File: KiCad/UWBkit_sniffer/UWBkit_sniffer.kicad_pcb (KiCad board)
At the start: 4 copper layers, 57.4 x 67.3 mm, 78 parts, among them J1 Conn_I2C1, J10 USB_C_Receptacle_USB2.0_14P, J11 USB_C_Receptacle_USB2.0_14P, J2 Conn_I2C2, J3 Conn_01x03, J4 Conn_SPIS, J5 Conn_SPIM, J6 Conn_SWD, J7 Conn_GPIO, J8 Conn_Coaxial, J9 Conn_01x02, SW1 SW_Push, T1 TestPoint_Small, T10 TestPoint_Small, T11 TestPoint_Small, T12 TestPoint_Small, T2 TestPoint_Small, T3 TestPoint_Small, T4 TestPoint_Small, T5 TestPoint_Small, T6 TestPoint_Small, T7 TestPoint_Small, T8 TestPoint_Small, T9 TestPoint_Small, U1 LBUA5QJ2AB, U2 XC9285B33CMR-G, U3 CP2104, U4 IP4234CZ6, U5 IP4234CZ6

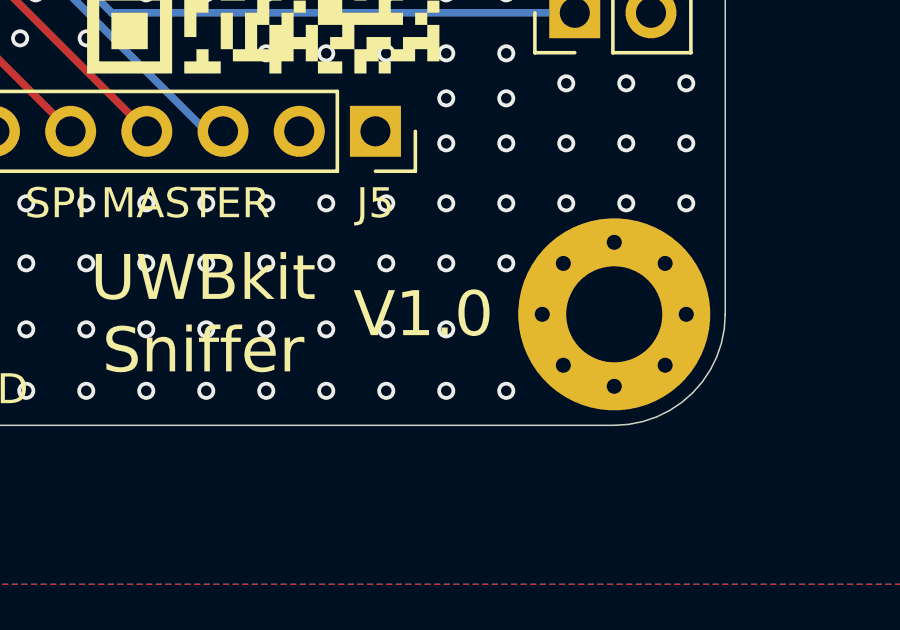
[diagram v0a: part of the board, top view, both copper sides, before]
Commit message: Fixed bottom silkscreen positioning for release V1.1
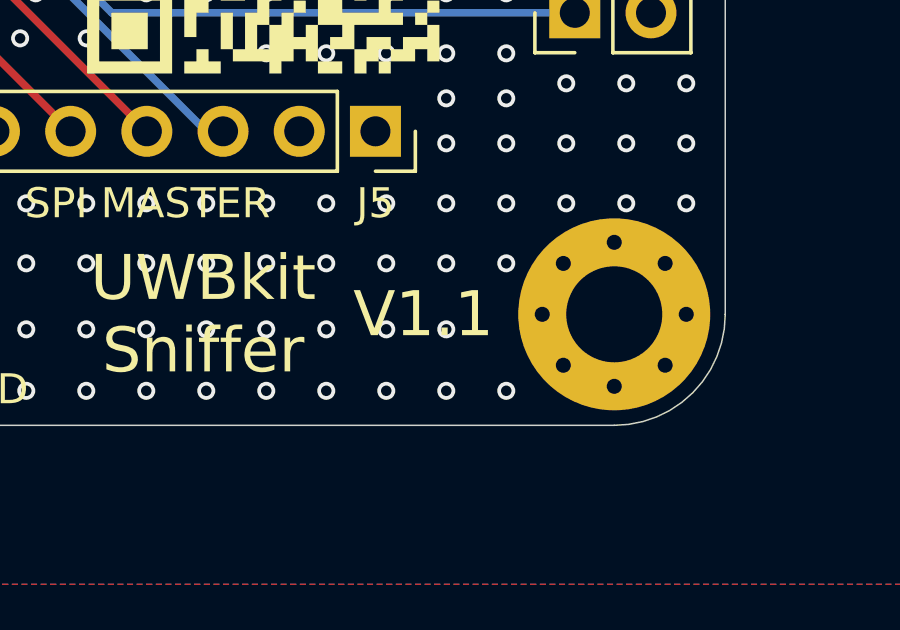
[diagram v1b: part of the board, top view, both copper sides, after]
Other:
- board text added: "V1.1"
- board text removed: "V1.0"
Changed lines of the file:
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@@
 		(tags "resistor")
 		(property "Reference" "R7"
-			(at -2.15 -0.55 0)
+			(at -2.95 0.015 90)
 			(layer "B.SilkS")
 			(effects
@@
 		(tags "resistor")
 		(property "Reference" "R1"
-			(at 2.15 -0.55 0)
+			(at 2.85 0.045 90)
 			(layer "B.SilkS")
 			(effects
@@
 		(tags "capacitor tantalum")
 		(property "Reference" "C10"
-			(at 0 0 90)
+			(at 0.0275 -1.740868 90)
 			(layer "B.SilkS")
 			(effects
@@
 		(tags "resistor")
 		(property "Reference" "R13"
-			(at 2.05 0.75 0)
+			(at -3.05 0.02 90)
 			(layer "B.SilkS")
 			(effects
@@
 		(tags "resistor")
 		(property "Reference" "R2"
-			(at -2.05 0.55 0)
+			(at 2.95 -0.04 90)
 			(layer "B.SilkS")
 			(effects
@@
 		(tags "capacitor")
 		(property "Reference" "C9"
-			(at 0.1225 -0.5 0)
+			(at 2.95 -0.008368 90)
 			(layer "B.SilkS")
 			(effects
@@
 		)
 	)
-	(gr_text "V1.0"
+	(gr_text "V1.1"
 		(locked yes)
 		(at 176.9 109.7 0)
@@
 			(justify left)
 		)
-		(render_cache "V1.0" 0
+		(render_cache "V1.1" 0
 			(polygon
 				(pts
@@
 			(polygon
 				(pts
-					(xy 181.656194 108.968013) (xy 181.694178 108.984146) (xy 181.729047 109.01174) (xy 181.75633 109.046877)
-					(xy 181.772343 109.085317) (xy 181.777773 109.128335) (xy 181.777773 110.15672) (xy 181.772303 110.200448)
-					(xy 181.756255 110.23908) (xy 181.729047 110.273956) (xy 181.694184 110.301054) (xy 181.655551 110.317047)
-					(xy 181.61181 110.3225) (xy 181.076827 110.3225) (xy 181.032435 110.31701) (xy 180.993643 110.300985)
-					(xy 180.959041 110.273956) (xy 180.932162 110.239119) (xy 180.916282 110.200485) (xy 180.910864 110.15672)
-					(xy 180.910864 110.152506) (xy 181.083055 110.152506) (xy 181.607689 110.152506) (xy 181.607689 109.13841)
-					(xy 181.083055 109.13841) (xy 181.083055 110.152506) (xy 180.910864 110.152506) (xy 180.910864 109.128335)
-					(xy 180.916337 109.085347) (xy 180.932489 109.04691) (xy 180.960048 109.01174) (xy 180.995277 108.984183)
-					(xy 181.033775 108.968029) (xy 181.076827 108.962555) (xy 181.613825 108.962555)
-				)
-			)
+					(xy 180.994945 110.152506) (xy 181.259276 110.152506) (xy 181.259276 109.132548) (xy 180.998975 109.132548)
+					(xy 180.965699 109.126336) (xy 180.937975 109.107819) (xy 180.91916 109.080358) (xy 180.912879 109.047552)
+					(xy 180.919163 109.014762) (xy 180.937975 108.987377) (xy 180.965706 108.968788) (xy 180.998975 108.962555)
+					(xy 181.431376 108.962555) (xy 181.431376 110.152506) (xy 181.603567 110.152506) (xy 181.603567 109.793195)
+					(xy 181.609796 109.76072) (xy 181.628663 109.732653) (xy 181.656459 109.71342) (xy 181.689663 109.707008)
+					(xy 181.722831 109.713296) (xy 181.750571 109.732103) (xy 181.769375 109.759767) (xy 181.775667 109.79292)
+					(xy 181.775667 110.236587) (xy 181.769378 110.269756) (xy 181.750571 110.297495) (xy 181.722826 110.316227)
+					(xy 181.689571 110.3225) (xy 180.994945 110.3225) (xy 180.961748 110.316067) (xy 180.933945 110.296762)
+					(xy 180.915097 110.268467) (xy 180.908849 110.235488) (xy 180.915101 110.203643) (xy 180.933945 110.176778)
+					(xy 180.961633 110.158618)
+				)
+			)
